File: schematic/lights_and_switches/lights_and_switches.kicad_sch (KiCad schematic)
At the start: 37 parts, among them U1 PIC16F884-IP

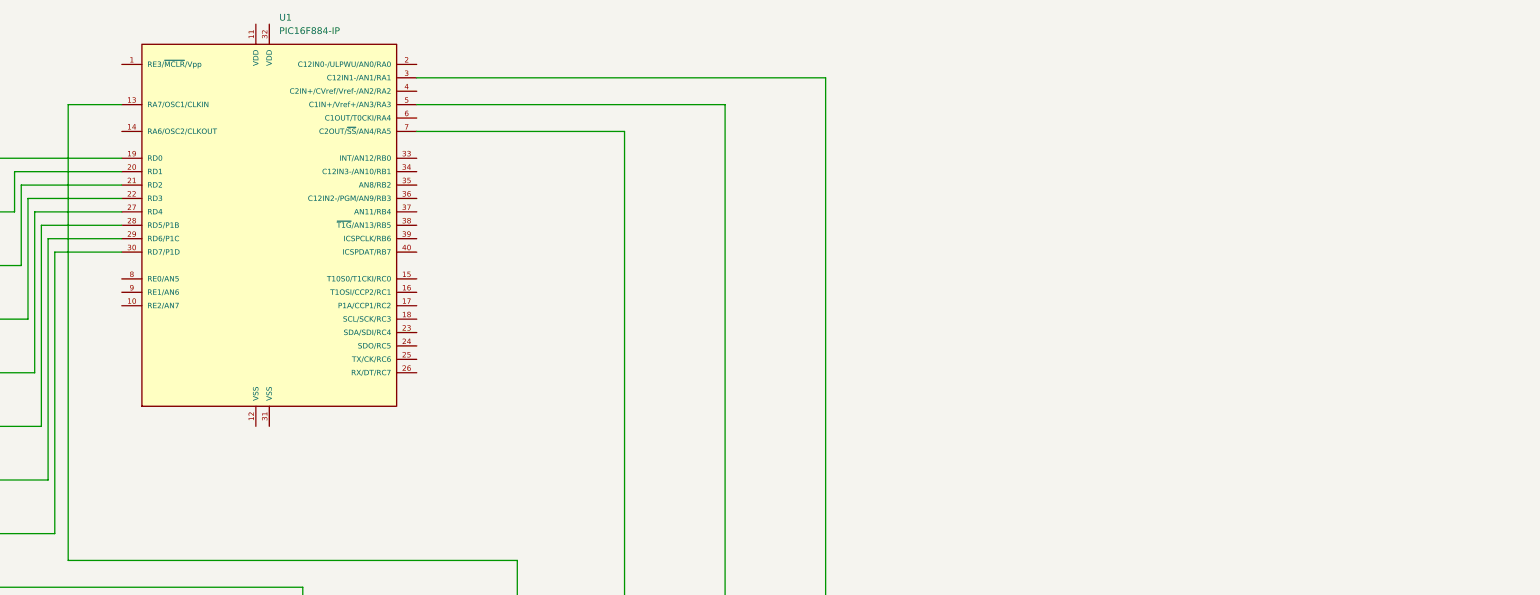
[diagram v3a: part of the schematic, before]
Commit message: Adding more wiring to schematic
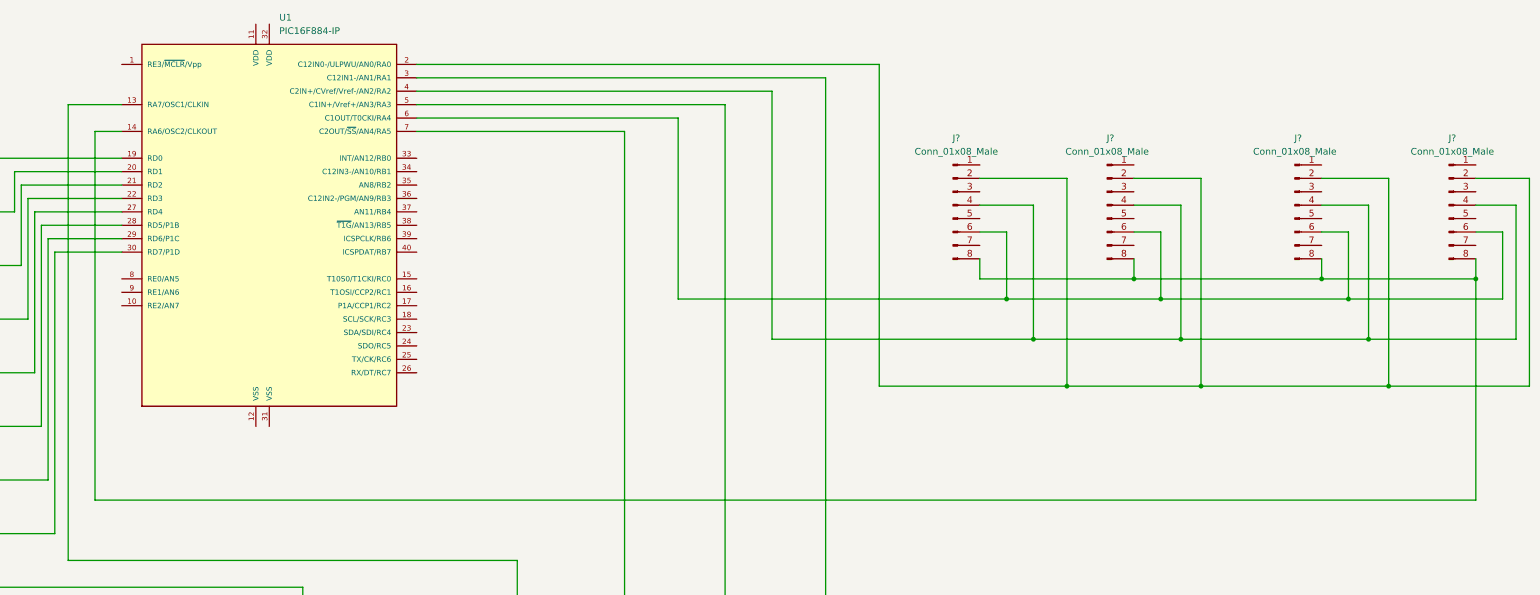
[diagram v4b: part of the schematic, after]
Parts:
- added J? (x4): Conn_01x08_Male, Connector_PinHeader_2.54mm:PinHeader_1x08_P2.54mm_Vertical, symbol Connector:Conn_01x08_Male
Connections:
- net at U1.14 (RA6/OSC2/CLKOUT): now also J?.8 (Pin_8), J?.8 (Pin_8), J?.8 (Pin_8), J?.8 (Pin_8)
- net at U1.2 (C12IN0-/ULPWU/AN0/RA0): now also J?.2 (Pin_2), J?.2 (Pin_2), J?.2 (Pin_2), J?.2 (Pin_2)
- net at U1.4 (C2IN+/CVref/Vref-/AN2/RA2): now also J?.4 (Pin_4), J?.4 (Pin_4), J?.4 (Pin_4), J?.4 (Pin_4)
- net at U1.6 (C1OUT/T0CKI/RA4): now also J?.6 (Pin_6), J?.6 (Pin_6), J?.6 (Pin_6), J?.6 (Pin_6)
